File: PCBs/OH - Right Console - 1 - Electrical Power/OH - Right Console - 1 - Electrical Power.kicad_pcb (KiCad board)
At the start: 2 copper layers, 59.9 x 33.3 mm, 15 parts, among them J1 Switch Inputs, J2 Batt U Volts In, J3 Batt E Volts In, J4 Batt U Volts Out, J5 Batt U Volts Out, SW1 EXT PWR, SW2 R GEN, SW3 L GEN

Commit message: Elect Power Done
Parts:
- moved H1 53.6 mm to (138.9, 99.3)
- moved H4 51.6 mm to (172.1, 85.5)
- moved J3 49.1 mm to (133.2, 90.8)
- moved J2 48.6 mm to (146.8, 91.1)
- moved J5 48.1 mm to (133.2, 82.0)
- moved J4 47.9 mm to (146.8, 82.0)
- moved SW3 44.8 mm to (160.3, 93.3)
- moved D1 36.5 mm to (120.7, 79.7), turned to 270 degrees
- moved D2 33.9 mm to (116.2, 79.7), turned to 270 degrees
- moved D3 32.4 mm to (102.7, 88.4), turned to 270 degrees
- moved J1 23.3 mm to (103.9, 82.0)
- moved H2 22.9 mm to (84.2, 99.7)
- moved H3 18.3 mm to (126.7, 82.8)
- moved SW1 12.6 mm to (116.2, 93.3)
- moved SW2 1.33 mm to (93.0, 100.2)
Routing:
- net Net-(D1-Pad1): track 8.01 -> 45.3 mm
- net Net-(D3-Pad1): track 38.1 -> 17.9 mm
- net /Row1: track 46.0 -> 63.4 mm
- net /Row2: track 33.0 -> 44.9 mm
- net Net-(D2-Pad1): track 26.6 -> 14.7 mm
- net Net-(D1-Pad2): track 27.0 -> 18.9 mm
- net Net-(D3-Pad2): track 18.8 -> 15.5 mm
- net Net-(J3-Pad4): track 10.4 -> 8.76 mm
- net Net-(J3-Pad3): track 10.4 -> 8.76 mm
- net Net-(J3-Pad2): track 10.4 -> 8.76 mm
- net Net-(J3-Pad1): track 10.4 -> 8.76 mm
- net Net-(J2-Pad4): track 10.3 -> 9.02 mm
- net Net-(J2-Pad3): track 10.3 -> 9.02 mm
- net Net-(J2-Pad2): track 10.3 -> 9.02 mm
- net Net-(J2-Pad1): track 10.3 -> 9.02 mm
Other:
- board size 59.9 x 33.3 mm -> 95.4 x 26.2 mm

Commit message: Panel refinement
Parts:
- J5: value Batt U Volts Out -> Batt E Volts Out
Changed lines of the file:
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@@
       (effects (font (size 1 1) (thickness 0.15)))
     )
-    (fp_text value "Batt U Volts Out" (at 3.81 4.08) (layer F.SilkS)
+    (fp_text value "Batt E Volts Out" (at 3.81 4.08) (layer F.SilkS)
       (effects (font (size 1 1) (thickness 0.15)))
     )

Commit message: PCBs
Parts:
- J2, J3, J4, J5: footprint PT_Library_v001:Molex_1x04_P2.54mm_Vertical -> PT_Library_v001:Molex_1x03_P2.54mm_Vertical
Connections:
- net Net-(J2-Pad1) renamed /U_PWM
- net Net-(J2-Pad2) renamed /U_5V
- net Net-(J2-Pad3) renamed /U_GND
- net Net-(J3-Pad1) renamed /E_PWM
- net Net-(J3-Pad2) renamed /E_5V
- net Net-(J3-Pad3) renamed /E_GND
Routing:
- net Net-(J2-Pad4): track 9.02 -> 0.00 mm
- net Net-(J3-Pad4): track 8.76 -> 0.00 mm
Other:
- board text added: "5V"
- board text added: "GND"
- board text added: "PWM"

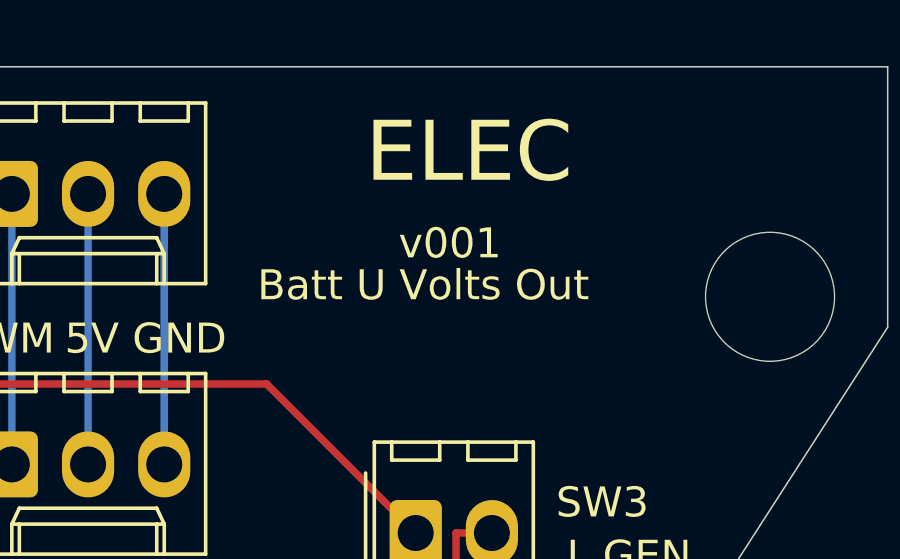
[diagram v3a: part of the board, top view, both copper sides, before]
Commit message: ELECT PANEL FIX
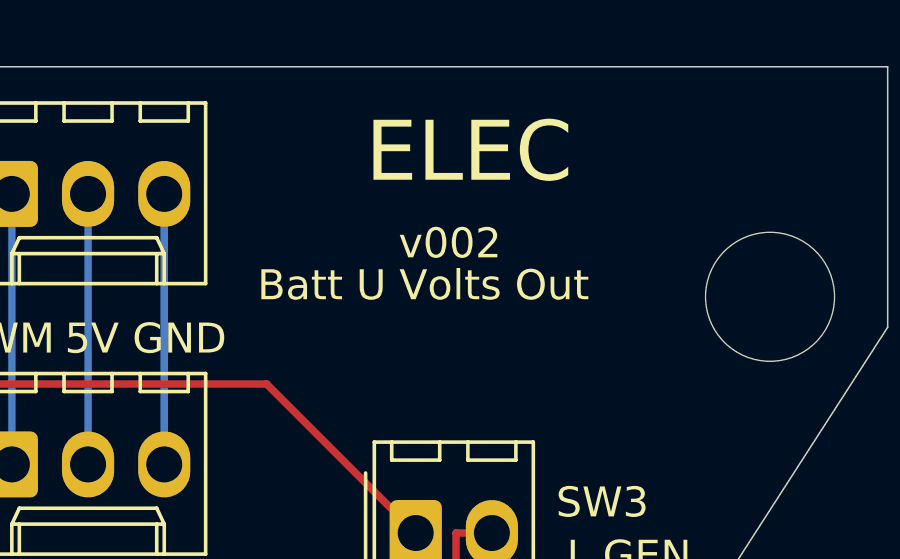
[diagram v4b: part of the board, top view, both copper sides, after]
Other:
- board text added: "v002"
- board text removed: "v001"
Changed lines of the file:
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@@
   (gr_line (start 100.076 77.804) (end 100.076 96.139) (layer Edge.Cuts) (width 0.05))
   (gr_line (start 176.006 77.804) (end 100.076 77.804) (layer Edge.Cuts) (width 0.05))
-  (gr_text v001 (at 161.417 83.693) (layer F.SilkS)
+  (gr_text v002 (at 161.417 83.693) (layer F.SilkS)
     (effects (font (size 1 1) (thickness 0.15)))
   )

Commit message: ELECTRICAL POWER
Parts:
- added J6: BACKLIGHT, PT_Library_v001:Molex_1x02_P2.54mm_Vertical, F.Cu at (104.5, 98.9)
- added J7: BACKLIGHT, PT_Library_v001:Molex_1x02_P2.54mm_Vertical, F.Cu at (112.9, 98.9)
- added J8: BACKLIGHT, PT_Library_v001:Molex_1x02_P2.54mm_Vertical, F.Cu at (121.2, 98.9)
- added J9: BACKLIGHT, PT_Library_v001:Molex_1x02_P2.54mm_Vertical, F.Cu at (129.5, 98.9)
- moved SW1 10.1 mm to (106.4, 90.7)
- moved D3 8.83 mm to (101.7, 79.6)
- moved J1 1.34 mm to (105.2, 82.0)
- moved J3 0.25 mm to (133.2, 90.6)
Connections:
- D2 pad 2: Net-(D1-Pad2) -> Net-(D2-Pad2)
- D3 pad 2: Net-(D3-Pad2) -> Net-(D1-Pad2)
- J1 pad 2: Net-(D3-Pad2) -> Net-(D2-Pad2)
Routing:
- net /BACKLIGHT-GND: track 0.00 -> 30.3 mm
- net /BACKLIGHT+12V: track 0.00 -> 28.6 mm
- net Net-(D3-Pad2): track 15.5 -> 0.00 mm
- net Net-(D2-Pad2): track 0.00 -> 11.0 mm
- net /Row2: track 44.9 -> 35.7 mm
- net /Row1: track 63.4 -> 72.3 mm
- net Net-(D3-Pad1): track 17.9 -> 26.3 mm
- net Net-(D1-Pad2): track 18.9 -> 24.8 mm
- net Net-(D2-Pad1): track 14.7 -> 20.4 mm
- net Net-(D1-Pad1): track 45.3 -> 45.9 mm
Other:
- board text added: "v003"
- board text removed: "v002"
